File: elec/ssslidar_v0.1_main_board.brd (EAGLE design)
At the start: 26 x 26 mm, 3 parts

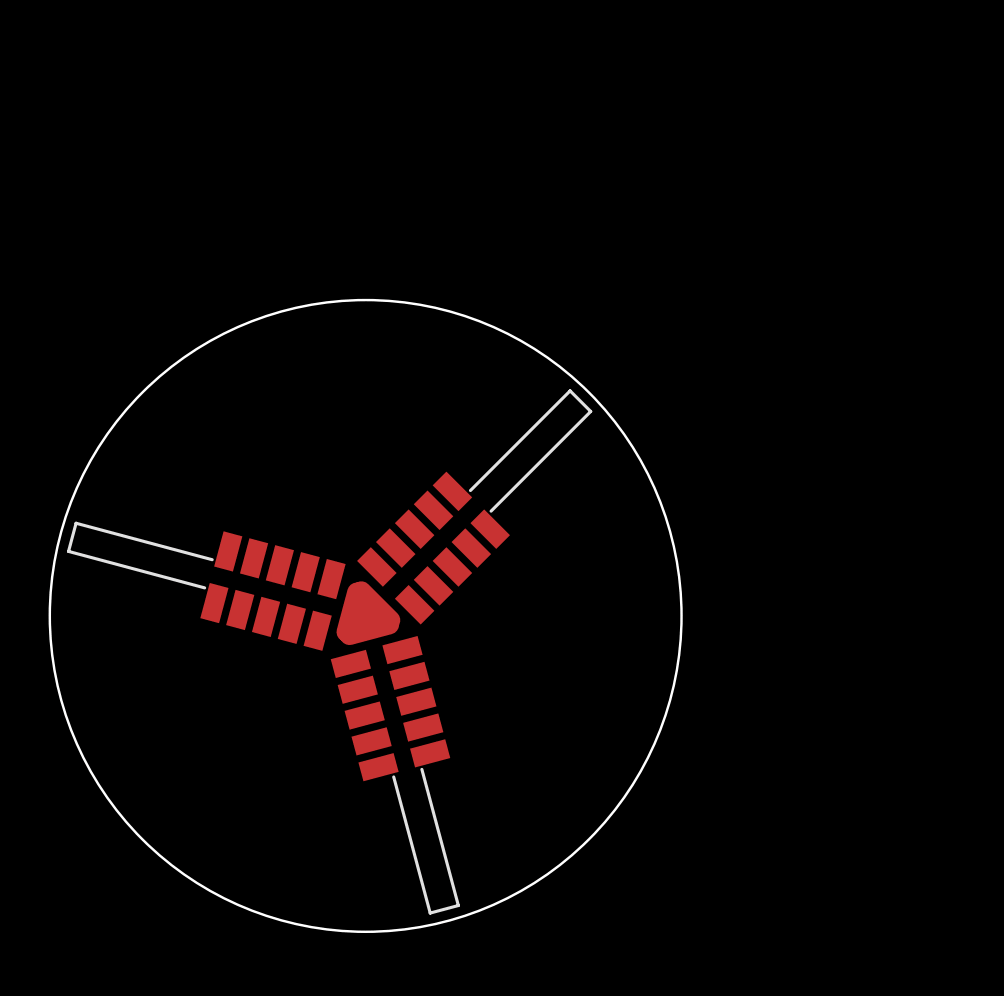
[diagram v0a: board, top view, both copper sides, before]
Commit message: Working on main board Made blades longer to avoid too much occlusion from the main PCB (but we will still need to put the whole thing on a mast).
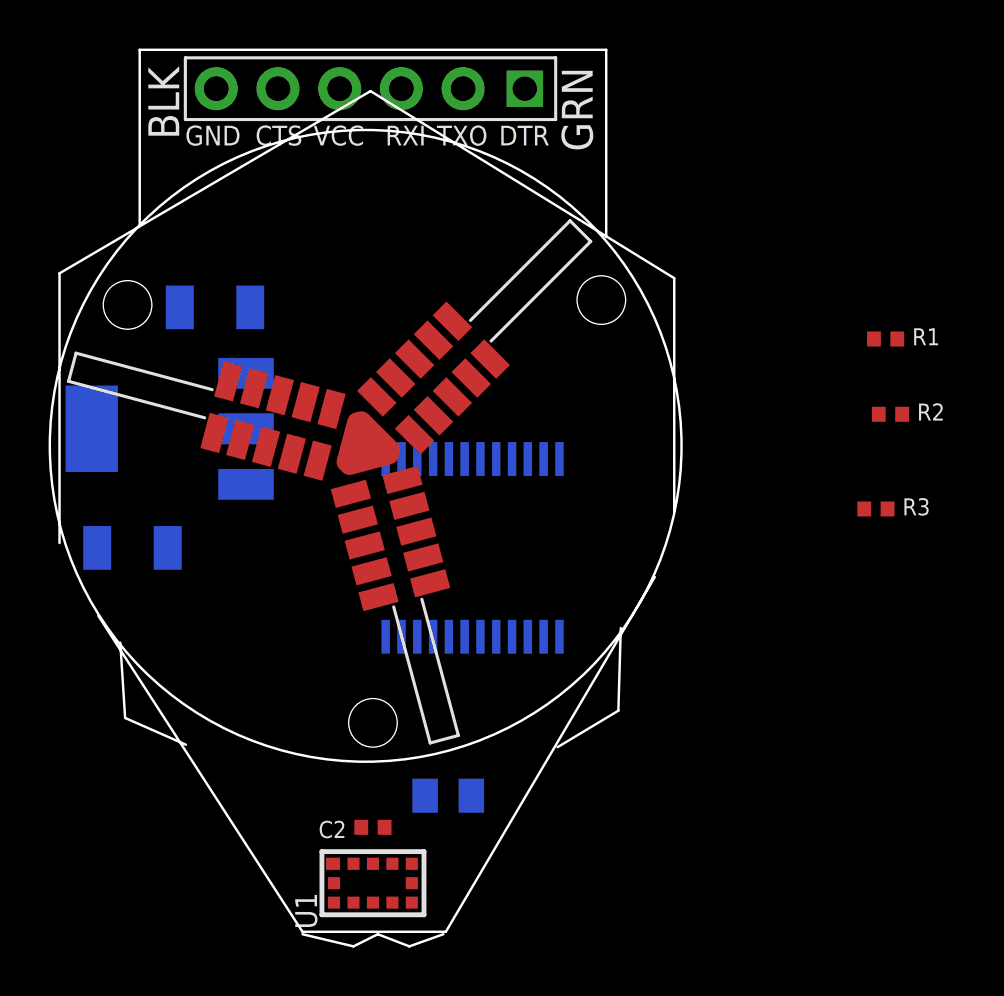
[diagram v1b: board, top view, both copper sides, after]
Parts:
- added C1: 10uF, Xevelabs:0805_N
- added C2: 100nF, Xevelabs:0402_N
- added C3, C4: (no value), Xevelabs:1206_N
- added JP1: FTDI_DEVICE, SparkFun-Connectors:FTDI_DEVICE_SIDE
- added R1, R2, R3: (no value), Xevelabs:0402_N
- added U$1: 74HC4067DB,118, SparkFun-AnalogIC:SSOP24
- added U1: VL53L0X, VL53L0X:VL53L0X
- added U2: TLV1117LV28DCYR, OPL:SOT223
- moved B1 7.00 mm to (13.0, 20.0)
- moved B2 7.00 mm to (13.0, 20.0)
- moved B3 7.00 mm to (13.0, 20.0)
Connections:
- new net !SDA_MUX_EN: U$1.15
- new net +5V: C3.1, U2.3
- new net G_INT1: U1.7
- new net G_SDA1: R3.1, U$1.19, U1.9
- new net SDA: R1.1, U$1.1
- new net SDA_ADDR0: U$1.10
- new net SDA_ADDR1: U$1.11
- new net SDA_ADDR2: U$1.14
- new net SDA_ADDR3: U$1.13
- net A_SDA1: now also U$1.9
- net A_SDA2: now also U$1.8
- net B_SDA1: now also U$1.7
- net B_SDA2: now also U$1.6
- net C_SDA1: now also U$1.5
- net C_SDA2: now also U$1.4
- net D_SDA1: now also U$1.3
- net D_SDA2: now also U$1.2
- net E_SDA1: now also U$1.23
- net E_SDA2: now also U$1.22
- net F_SDA1: now also U$1.21
- net F_SDA2: now also U$1.20
- net GND: now also C1.2, C2.2, C3.2, C4.2, JP1.P$5, U$1.12, U1.12, U1.2, U1.3, U1.4, U1.6, U2.1
- net SCL: now also R2.1, U1.10
- net VDD: now also C1.1, C2.1, C4.1, R1.2, R2.2, R3.2, U$1.24, U1.1, U1.11, U1.5, U2.2, U2.TER
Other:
- board size 26 x 26 mm -> 26 x 36.9 mm

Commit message: Updated blades (ready for release). Double power rail for sensors.
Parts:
- removed R1: (no value), Xevelabs:0402_N
- removed U2: TLV1117LV28DCYR, OPL:SOT223
- added C10, C9: 6pF, Xevelabs:0201_N
- added C12, C8: 4.7uF 10V, Xevelabs:0603_N
- added C13, C14: 100nF, Xevelabs:0201_N
- added C16: 470pF, Xevelabs:0201_N
- added C5, C6: (no value), Xevelabs:1206_N
- added C7: 10uF 25V, Xevelabs:0805_N
- added JP3: DXL_EXT, SparkFun-Connectors:1X06-1.27MM
- added LED1: yellow, Xevelabs:D_0603_L
- added P1, P10, P11, P12, P14, P15, P2, P3, P4, P5, P6, P7: PIN_SMD_0.8X1.6, Xevelabs:PIN_SMD_0.8X1.6
- added Q1: XRCGB24M000F3M00R0 (24MHz), Xevelabs:CRYSTAL_2.0X1.6_4P
- added R6: 470, Xevelabs:0201_N
- added U$2: 74HC4067DB,118, SparkFun-AnalogIC:SSOP24
- added U3: MIC5235-5.0YM5, SparkFun-PowerIC:SOT23-5
- added U4: STM32F301K6U6, stm32F301:QFN50P500X500X60-33N
- added U7: MIC5205-3.3YM5, OPL:SC70-5
- R2, R3: value (none) -> 2k
- moved U$1 32.3 mm to (30.1, 45.5), turned to 90 degrees
- moved C3 5.38 mm to (2.80, 22.1)
- moved C4 1.92 mm to (4.60, 14.3)
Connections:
- removed net !SDA_MUX_EN: U$1.15
- removed net SDA_ADDR0: U$1.10
- removed net SDA_ADDR1: U$1.11
- removed net SDA_ADDR2: U$1.14
- removed net SDA_ADDR3: U$1.13
- new net !MUX_EN: U$1.15, U$2.15
- new net +12V: C7.1, U3.1, U3.3
- new net +3V3: C12.1, C13.1, C14.1, LED1.A, P10.PIN, U4.1, U4.17, U4.5, U7.5
- new net COM_RST: P14.PIN, U4.4
- new net COM_RX: U4.19
- new net COM_TX: U4.20
- new net DBG_GPIO1: P3.PIN, U4.27
- new net DBG_GPIO2: P7.PIN, U4.8
- new net DBG_GPIO3: P6.PIN, U4.7
- new net DBG_RX: P5.PIN, U4.25
- new net DBG_TX: P4.PIN, U4.26
- new net DXL<MCU: JP3.2
- new net DXL>MCU: JP3.1
- new net IMU_SCL: U4.18
- new net IMU_SDA: U4.28
- new net INT: U$2.1
- new net LED: R6.2, U4.30
- new net MPU_INT: U4.21
- new net MUX_ADDR0: U$1.10, U$2.10
- new net MUX_ADDR1: U$1.11, U$2.11
- new net MUX_ADDR2: U$1.14, U$2.14
- new net MUX_ADDR3: U$1.13, U$2.13
- new net N$1: C10.1, Q1.1, U4.2
- new net N$10: JP3.4
- new net N$11: JP3.6
- new net N$2: C9.1, Q1.3, U4.3
- new net N$4: LED1.C, R6.1
- new net N$7: C16.1, U7.4
- new net N$9: JP3.3
- new net RX_EN: U4.22
- new net SWCLK: P11.PIN, U4.24
- new net SWDIO: P12.PIN, U4.23
- new net VEE: B1.3, C1.1, C2.1, C6.1, R3.2, U1.1, U1.11
- net +5V: now also C5.1, C8.1, U3.5, U7.1, U7.3; no longer U2.3
- net A_INT1: now also B1.5, U$2.9; no longer B1.4
- net A_INT2: now also U$2.8
- net A_SDA1: now also B1.4; no longer B1.3
- net B_INT1: now also U$2.7
- net B_INT2: now also U$2.6
- net C_INT1: now also U$2.5
- net C_INT2: now also U$2.4
- net D_INT1: now also U$2.3
- net D_INT2: now also U$2.2
- net E_INT1: now also U$2.23
- net E_INT2: now also U$2.22
- net F_INT1: now also U$2.21
- net F_INT2: now also U$2.20
- net GND: now also C10.2, C12.2, C13.2, C14.2, C16.2, C5.2, C6.2, C7.2, C8.2, C9.2, JP3.5, P1.PIN, P15.PIN, P2.PIN, Q1.2, Q1.4, U$2.12, U3.2, U4.16, U4.31, U4.32, U4.33, U4.6, U7.2; no longer U2.1
- net G_INT1: now also U$2.19
- net SDA: no longer R1.1
- net VDD: now also U$2.24; no longer C1.1, C2.1, R1.2, R3.2, U1.1, U1.11, U2.2, U2.TER

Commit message: Main board outline and schematics nearly ready
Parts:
- removed C12, C8: 4.7uF 10V, Xevelabs:0603_N
- removed C16: 470pF, Xevelabs:0201_N
- removed P1: PIN_SMD_0.8X1.6, Xevelabs:PIN_SMD_0.8X1.6
- removed U3: MIC5235-5.0YM5, SparkFun-PowerIC:SOT23-5
- removed U7: MIC5205-3.3YM5, OPL:SC70-5
- added C11: 22uF, Xevelabs:1206_L
- added D1, D2: (no value), OPL:SOD123
- added IC1, IC2: MIC5504-2.8YM5, v-reg-micrel:SOT23-5
- added JP2: EXT_PWR, pinhead:1X02
- added L2: VLS2012ET-2R2M, Xevelabs:2016_METRIC_N
- added P8: PIN_SMD_0.8X1.6, Xevelabs:PIN_SMD_0.8X1.6
- added U2: TPS62173DSG, Xevelabs:SON50P200X200X80-9L
- C7: value 10uF 25V -> 22uF@16V; device Xevelabs:0805_N -> Xevelabs:1206_L
- moved C6 46.2 mm to (16.9, 32.4), flipped to the bottom, turned to 270 degrees
- moved C7 40.5 mm to (11.9, 35.5), flipped to the bottom, turned to 180 degrees
- moved C5 34.9 mm to (22.1, 19.7), flipped to the bottom, turned to 270 degrees
- moved U4 28.4 mm to (15.6, 16.0), flipped to the bottom
- moved U$2 22.2 mm to (4.60, 28.1), turned to 0 degrees
- moved U$1 18.4 mm to (25.5, 27.7), turned to 0 degrees
- moved JP3 10.4 mm to (15.8, 38.2)
- moved C3 7.78 mm to (8.30, 16.6)
- moved JP1 7.23 mm to (15.0, 41.7)
- moved C4 6.89 mm to (7.80, 20.4), turned to 90 degrees
- moved B1 5.39 mm to (15.0, 25.0)
- moved B2 5.39 mm to (15.0, 25.0)
- moved B3 5.39 mm to (15.0, 25.0)
- moved R2 5.39 mm to (36.6, 26.3)
- moved R3 5.39 mm to (36.0, 22.4)
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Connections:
- removed net +3V3: C12.1, C13.1, C14.1, LED1.A, P10.PIN, U4.1, U4.17, U4.5, U7.5
- removed net COM_RX: U4.19
- removed net COM_TX: U4.20
- removed net IMU_SCL: U4.18
- removed net IMU_SDA: U4.28
- removed net MPU_INT: U4.21
- removed net N$10: JP3.4
- removed net N$11: JP3.6
- removed net N$9: JP3.3
- removed net RX_EN: U4.22
- new net DBG_GPIO4: P8.PIN
- new net N$3: L2.1, U2.7
- new net N$5: C7.1, D1.-, U2.2, U2.3
- new net RXD: JP1.P$3
- new net TXD: JP1.P$2
- net +12V: now also D1.+, JP2.1, JP3.6; no longer C7.1, U3.1, U3.3
- net +5V: now also D2.+, JP1.P$4; no longer C3.1, C5.1, C8.1, U3.5, U7.1, U7.3
- net DBG_GPIO1: no longer U4.27
- net DBG_GPIO2: no longer U4.8
- net DBG_GPIO3: no longer U4.7
- net DBG_RX: no longer U4.25
- net DBG_TX: no longer U4.26
- net GND: now also C11.2, IC1.2, IC2.2, JP1.P$6, JP2.2, U2.1, U2.4, U2.5, U2.9; no longer C12.2, C16.2, C8.2, P1.PIN, U3.2, U7.2
- net N$7: now also C11.1, C3.1, C5.1, D2.-, IC1.1, IC1.3, IC2.1, IC2.3, L2.2, U2.6; no longer C16.1, U7.4
- net VDD: now also C13.1, C14.1, IC2.5, LED1.A, P10.PIN, U4.1, U4.17, U4.5
- net VEE: now also IC1.5
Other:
- board size 26 x 36.9 mm -> 30 x 41.5 mm

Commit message: Added leds, finished sch
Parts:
- removed C1: 10uF, Xevelabs:0805_N
- removed C5: (no value), Xevelabs:1206_N
- removed LED1: yellow, Xevelabs:D_0603_L
- removed R6: 470, Xevelabs:0201_N
- added C8: 100nF, Xevelabs:0402_N
- added L1: Ferrite 10R BLM18BA100SN1D, Xevelabs:0603_N
- added LED10, LED11, LED12, LED13, LED14, LED3, LED4, LED5, LED6, LED7, LED8, LED9: yellow, Xevelabs:D_0603_L
- added LED2: Blue, Xevelabs:D_0603_L
- added P1, P13, P16, P17, P18, P19, P20, P21, P22, P23, P24, P25, P26, P27, P28, P9: PIN_SMD_0.8X1.6, Xevelabs:PIN_SMD_0.8X1.6
- added R1: 470, Xevelabs:0402_N
- added R4: 10k, Xevelabs:0402_N
- added R5, R7, R8, R9: TBD, Xevelabs:0402_N
- C10, C13, C14, C9: device Xevelabs:0201_N -> Xevelabs:0402_N
- C3, C4, C6: value (none) -> 10uF; device Xevelabs:1206_N -> Xevelabs:0805_N
- JP2: value EXT_PWR -> M021X02_NO_SILK; device pinhead:1X02 -> SparkFun-Connectors:1X02_NO_SILK
- P3, P6, P7, P8: value PIN_SMD_0.8X1.6 -> PIN_SMD_1X1; device Xevelabs:PIN_SMD_0.8X1.6 -> Xevelabs:PIN_SMD_1X1
- U2: device Xevelabs:SON50P200X200X80-9L -> Xevelabs:SON50P200X200X80-9N
- moved U4 44.8 mm to (59.9, 22.4), turned to 90 degrees
- moved P5 44.7 mm to (28.8, 19.5), turned to 180 degrees
- moved P6 44.3 mm to (44.1, 10.2), flipped to the bottom
- moved P4 42.7 mm to (28.8, 20.8), turned to 180 degrees
- moved P2 37.9 mm to (28.8, 25.9), turned to 180 degrees
- moved P3 37.8 mm to (45.5, 10.5), flipped to the bottom
- moved P10 37.6 mm to (28.8, 28.4), turned to 180 degrees
- moved P15 37.4 mm to (28.8, 23.3), turned to 180 degrees
- moved P11 36.9 mm to (28.8, 22.0), turned to 180 degrees
- moved P12 36.9 mm to (28.8, 24.6), turned to 180 degrees
- moved P14 36.9 mm to (28.8, 27.1), turned to 180 degrees
- moved C10 29.7 mm to (61.2, 17.5), flipped to the bottom
- moved P7 26.7 mm to (40.2, 11.2), flipped to the bottom
- moved D2 25.4 mm to (12.0, 36.5), turned to 180 degrees
- moved IC1 25.2 mm to (2.67, 29.7), turned to 0 degrees
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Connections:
- removed net DBG_RX: P5.PIN
- removed net DBG_TX: P4.PIN
- removed net LED: R6.2, U4.30
- removed net N$4: LED1.C, R6.1
- new net DTR: C8.1, JP1.P$1
- new net LED1: R5.1, U4.7
- new net LED2: R7.1, U4.8
- new net LED3: R8.1, U4.9
- new net LED4: R9.1, U4.10
- new net N$10: LED10.C, LED3.C, LED4.A, LED5.C, LED6.A, LED9.A, R7.2
- new net N$11: LED11.A, LED12.C, LED5.A, LED6.C, LED7.A, LED8.C, R8.2
- new net N$12: LED10.A, LED13.C, LED14.A, LED7.C, LED8.A, LED9.C, R9.2
- new net N$6: C11.1, L1.1, L2.2, U2.6
- new net N$8: LED2.C, R1.1
- new net N$9: LED11.C, LED12.A, LED13.A, LED14.C, LED3.A, LED4.C, R5.2
- net !MUX_EN: now also U4.15
- net +12V: now also JP2.2; no longer JP2.1
- net COM_RST: now also C8.2, R4.2
- net DBG_GPIO1: now also P3.P$1, U4.21; no longer P3.PIN
- net DBG_GPIO2: now also P7.P$1, U4.22; no longer P7.PIN
- net DBG_GPIO3: now also P6.P$1, U4.18; no longer P6.PIN
- net DBG_GPIO4: now also P8.P$1, U4.28; no longer P8.PIN
- net DXL<MCU: now also U4.26
- net DXL>MCU: now also U4.27
- net GND: now also JP2.1, R1.2; no longer C1.2, C5.2, JP2.2
- net INT: now also U4.25
- net MUX_ADDR0: now also U4.11
- net MUX_ADDR1: now also U4.12
- net MUX_ADDR2: now also U4.13
- net MUX_ADDR3: now also U4.14
- net N$7: now also L1.2, LED2.A; no longer C11.1, C5.1, L2.2, U2.6
- net RXD: now also P5.PIN, U4.30
- net SCL: now also U4.19
- net SDA: now also U4.20
- net TXD: now also P4.PIN, U4.29
- net VDD: now also R4.1; no longer LED1.A
- net VEE: no longer C1.1
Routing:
- added copper zone on layer 2, net GND
- added copper zone on layer 3, net VDD
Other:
- board size 30 x 41.5 mm -> 30 x 41 mm

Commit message: Routing WIP
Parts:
- added K1: BUTTON-2P-REINFORCE-3100060P1, OPL:4P-SMD-7.0X3.5X3.5H-90D
- B1: value (none) -> PWR
- B2, B3: value (none) -> SIG
- moved U$1 44.1 mm to (62.7, 32.5)
- moved U$2 37.0 mm to (46.5, 32.1)
- moved R7 36.7 mm to (15.8, 5.85), flipped to the bottom, turned to 270 degrees
- moved R5 31.8 mm to (19.8, 6.85), flipped to the bottom, turned to 225 degrees
- moved R8 28.5 mm to (10.2, 6.95), flipped to the bottom, turned to 315 degrees
- moved R9 27.5 mm to (14.2, 6.45), flipped to the bottom, turned to 90 degrees
- moved IC2 25.3 mm to (27.8, 21.5)
- moved C6 25.2 mm to (27.8, 24.5)
- moved IC1 25.2 mm to (27.8, 27.9)
- moved C4 24.5 mm to (27.0, 18.3)
- moved C13 23.9 mm to (35.8, 16.6), turned to 270 degrees
- moved C14 21.4 mm to (41.8, 22.6), turned to 0 degrees
- moved U4 20.7 mm to (39.5, 18.9), turned to 0 degrees
- moved C10 17.2 mm to (44.5, 21.6), turned to 0 degrees
- moved R1 16.5 mm to (5.65, 31.6)
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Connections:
- new net N$4: K1.1
- net GND: now also K1.2, K1.S1, K1.S2
- net VDD: no longer U1.5
- net VEE: now also U1.5
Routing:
- net N$11: track 0.00 -> 20.8 mm, vias 0 -> 2
- net GND: track 0.00 -> 15.7 mm, vias 0 -> 3
- net N$12: track 0.00 -> 13.2 mm
- net N$9: track 0.00 -> 13.1 mm
- net VEE: track 0.00 -> 11.8 mm, vias 0 -> 1
- net N$10: track 0.00 -> 9.69 mm
- net LED2: track 0.00 -> 5.39 mm, vias 0 -> 2
- net LED1: track 0.00 -> 4.53 mm
- net LED4: track 0.00 -> 4.44 mm, vias 0 -> 2
- net N$1: track 0.00 -> 4.38 mm
- net SCL: track 0.00 -> 3.65 mm
- net VDD: track 0.00 -> 3.61 mm
- net N$2: track 0.00 -> 3.33 mm
- net G_SDA1: track 0.00 -> 3.21 mm
- net G_INT1: track 0.00 -> 2.70 mm
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- added copper zone on layer 1, net GND
- added copper zone on layer 16, net GND
